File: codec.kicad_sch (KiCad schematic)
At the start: 27 parts, among them J10 FCR684204T, J11 DIN_DOUT_2TP, J13 AJ_TP5, J14 C_G0, J15 C_G7, J16 CRST, J17 C_CLKOUT, J5 RX0/RX1, U4 WM8805GEDS_V, Y2 12M

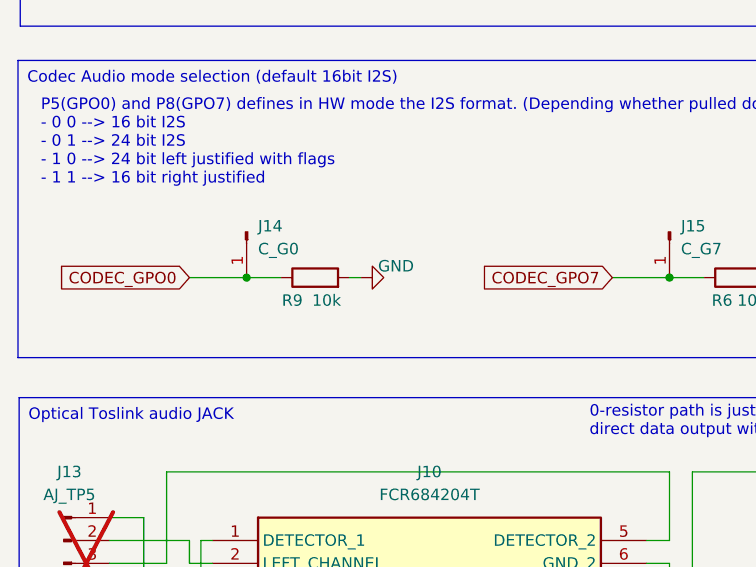
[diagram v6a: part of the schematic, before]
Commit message: component footprint updates
- 0402 caps and resistors to 0603
- reset pin-header to reset button

Signed-off-by: Mika Laitio <lamikr@gmail.com>
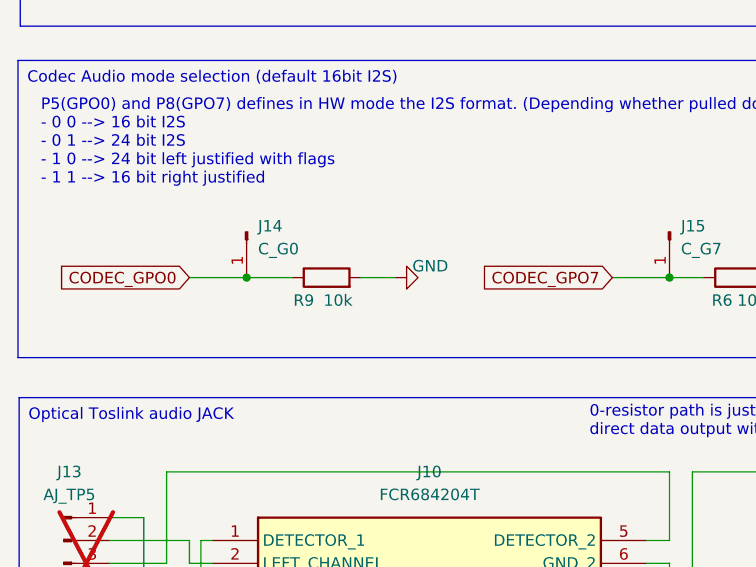
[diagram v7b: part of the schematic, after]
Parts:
- C17, C18, C19, C20, C21: footprint Capacitor_SMD:C_0402_1005Metric -> Capacitor_SMD:C_0603_1608Metric
- R6, R7, R8, R9: footprint Resistor_SMD:R_0402_1005Metric -> Resistor_SMD:R_0603_1608Metric
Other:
- moved on the sheet: R9
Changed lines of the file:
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@@
 	(wire
 		(pts
-			(xy 41.91 118.11) (xy 45.72 118.11)
+			(xy 41.91 118.11) (xy 46.99 118.11)
 		)
 		(stroke
@@
 	(wire
 		(pts
-			(xy 53.34 118.11) (xy 54.61 118.11)
+			(xy 54.61 118.11) (xy 58.42 118.11)
 		)
 		(stroke
@@
 			)
 		)
-		(property "Footprint" "Capacitor_SMD:C_0402_1005Metric"
+		(property "Footprint" "Capacitor_SMD:C_0603_1608Metric"
 			(at 64.4652 78.74 0)
 			(effects
@@
 			)
 		)
-		(property "Footprint" "Resistor_SMD:R_0402_1005Metric"
+		(property "Footprint" "Resistor_SMD:R_0603_1608Metric"
 			(at 58.42 57.658 90)
 			(effects
@@
 	(symbol
 		(lib_id "power:GND")
-		(at 54.61 118.11 90)
+		(at 58.42 118.11 90)
 		(unit 1)
 		(exclude_from_sim no)
@@
 		(dnp no)
 		(property "Reference" "#PWR029"
-			(at 60.96 118.11 0)
+			(at 64.77 118.11 0)
 			(effects
 				(font
@@
 		)
 		(property "Value" "GND"
-			(at 56.515 116.84 90)
+			(at 60.325 116.84 90)
 			(effects
 				(font
@@
 		)
 		(property "Footprint" ""
-			(at 54.61 118.11 0)
+			(at 58.42 118.11 0)
 			(effects
 				(font
@@
 		)
 		(property "Datasheet" ""
-			(at 54.61 118.11 0)
+			(at 58.42 118.11 0)
 			(effects
 				(font
@@
 		)
 		(property "Description" "Power symbol creates a global label with name \"GND\" , ground"
-			(at 54.61 118.11 0)
+			(at 58.42 118.11 0)
 			(effects
 				(font
@@
 			)
 		)
-		(property "Footprint" "Capacitor_SMD:C_0402_1005Metric"
+		(property "Footprint" "Capacitor_SMD:C_0603_1608Metric"
 			(at 256.54 137.4648 0)
 			(effects
@@
 			)
 		)
-		(property "Footprint" "Resistor_SMD:R_0402_1005Metric"
+		(property "Footprint" "Resistor_SMD:R_0603_1608Metric"
 			(at 181.61 117.348 90)
 			(effects
@@
 			)
 		)
-		(property "Footprint" "Capacitor_SMD:C_0402_1005Metric"
+		(property "Footprint" "Capacitor_SMD:C_0603_1608Metric"
 			(at 65.7352 33.02 0)
 			(effects
@@
 			)
 		)
-		(property "Footprint" "Capacitor_SMD:C_0402_1005Metric"
+		(property "Footprint" "Capacitor_SMD:C_0603_1608Metric"
 			(at 256.54 150.1648 0)
 			(effects
@@
 			)
 		)
-		(property "Footprint" "Resistor_SMD:R_0402_1005Metric"
+		(property "Footprint" "Resistor_SMD:R_0603_1608Metric"
 			(at 96.52 119.888 90)
 			(effects
@@
 			)
 		)
-		(property "Footprint" "Capacitor_SMD:C_0402_1005Metric"
+		(property "Footprint" "Capacitor_SMD:C_0603_1608Metric"
 			(at 92.4052 168.91 0)
 			(effects
@@
 	(symbol
 		(lib_id "Device:R")
-		(at 49.53 118.11 90)
+		(at 50.8 118.11 90)
 		(unit 1)
 		(exclude_from_sim no)
@@
 		(dnp no)
 		(property "Reference" "R9"
-			(at 46.99 120.65 90)
+			(at 48.26 120.65 90)
 			(effects
 				(font
@@
 		)
 		(property "Value" "10k"
-			(at 50.8 120.65 90)
+			(at 52.07 120.65 90)
 			(effects
 				(font
@@
 			)
 		)
-		(property "Footprint" "Resistor_SMD:R_0402_1005Metric"
-			(at 49.53 119.888 90)
+		(property "Footprint" "Resistor_SMD:R_0603_1608Metric"
+			(at 50.8 119.888 90)
 			(effects
 				(font
@@
 		)
 		(property "Datasheet" "~"
-			(at 49.53 118.11 0)
+			(at 50.8 118.11 0)
 			(effects
 				(font
@@
 		)
 		(property "Description" "Resistor"
-			(at 49.53 118.11 0)
+			(at 50.8 118.11 0)
 			(effects
 				(font
@@
 		)
 		(property "Notes" ""
-			(at 49.53 118.11 0)
+			(at 50.8 118.11 0)
 			(effects
 				(font
@@
 		)
 		(property "Price" "0.1"
-			(at 49.53 118.11 0)
+			(at 50.8 118.11 0)
 			(effects
 				(font
@@
 		)
 		(property "MFR" "Yageo"
-			(at 49.53 118.11 0)
+			(at 50.8 118.11 0)
 			(effects
 				(font
@@
 		)
 		(property "MPN" "RC0402FR-0710KL"
-			(at 49.53 118.11 0)
+			(at 50.8 118.11 0)
 			(effects
 				(font
@@
 		)
 		(property "SKU_DIGIKEY" "311-10.0KLRCT-ND"
-			(at 49.53 118.11 0)
+			(at 50.8 118.11 0)
 			(effects
 				(font
@@
 		)
 		(property "QtyOrdered" "100"
-			(at 49.53 118.11 0)
+			(at 50.8 118.11 0)
 			(effects
 				(font

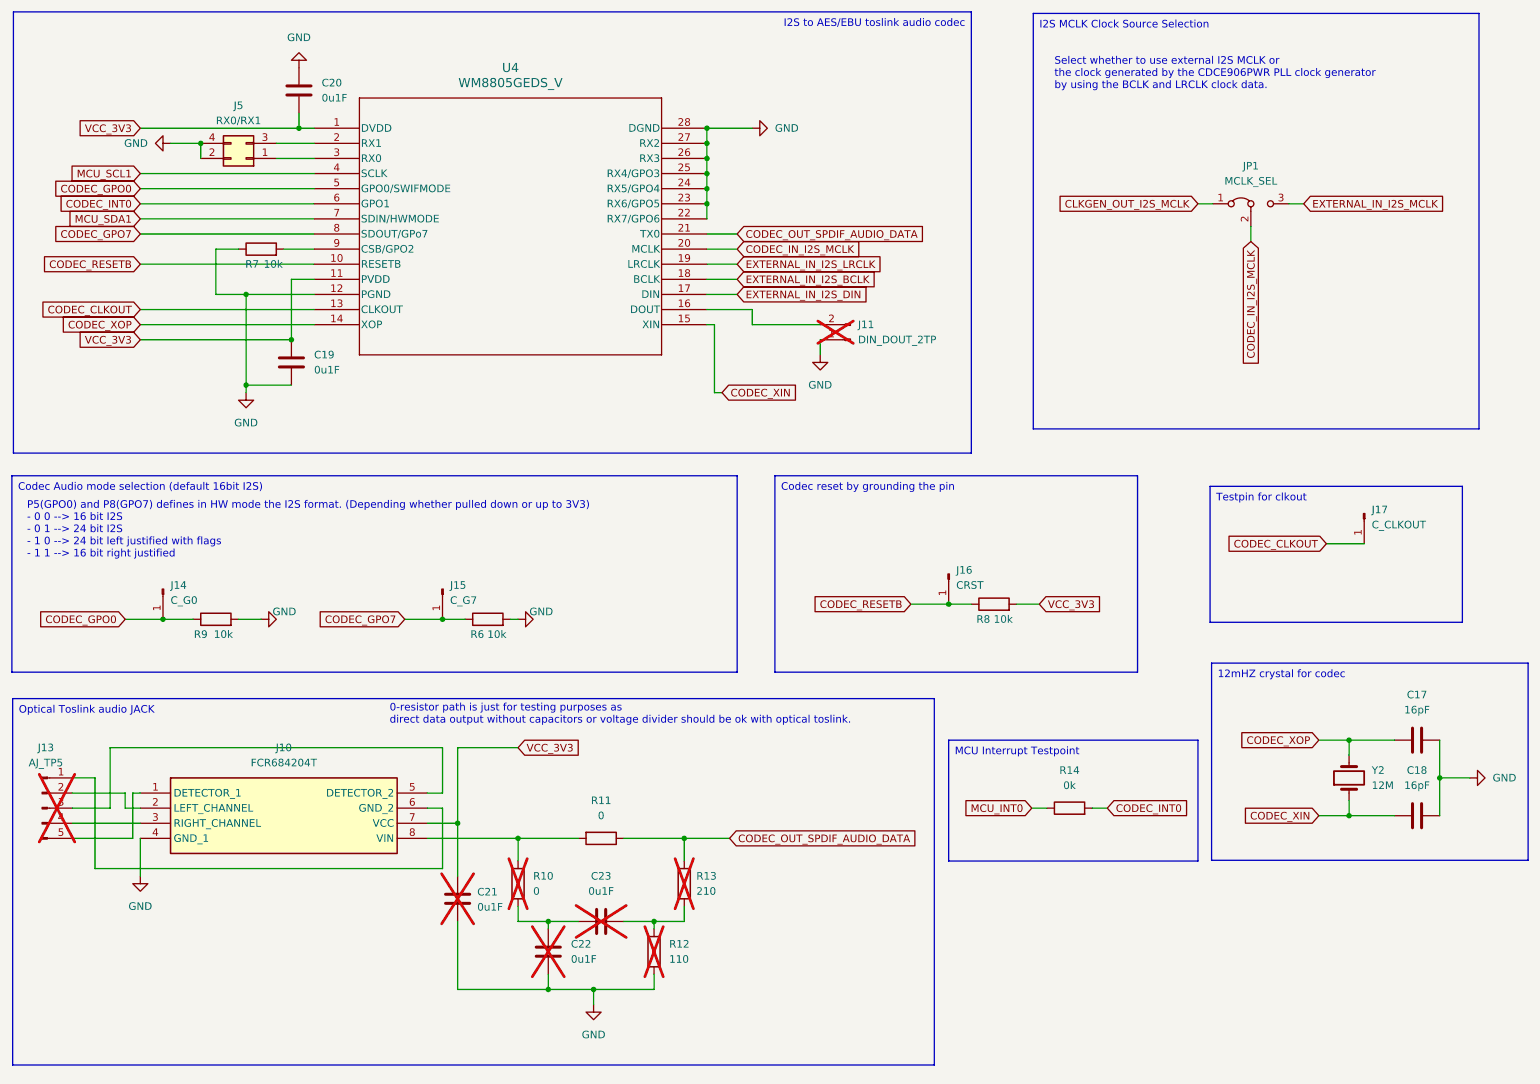
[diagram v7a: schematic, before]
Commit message: add pull-up resistors for codex rx-pins
- add connectors for rx0 and rx1 pins
- rest of the rx-pins not reserved for use
  and they will share a common pull-up.

Signed-off-by: Mika Laitio <lamikr@gmail.com>
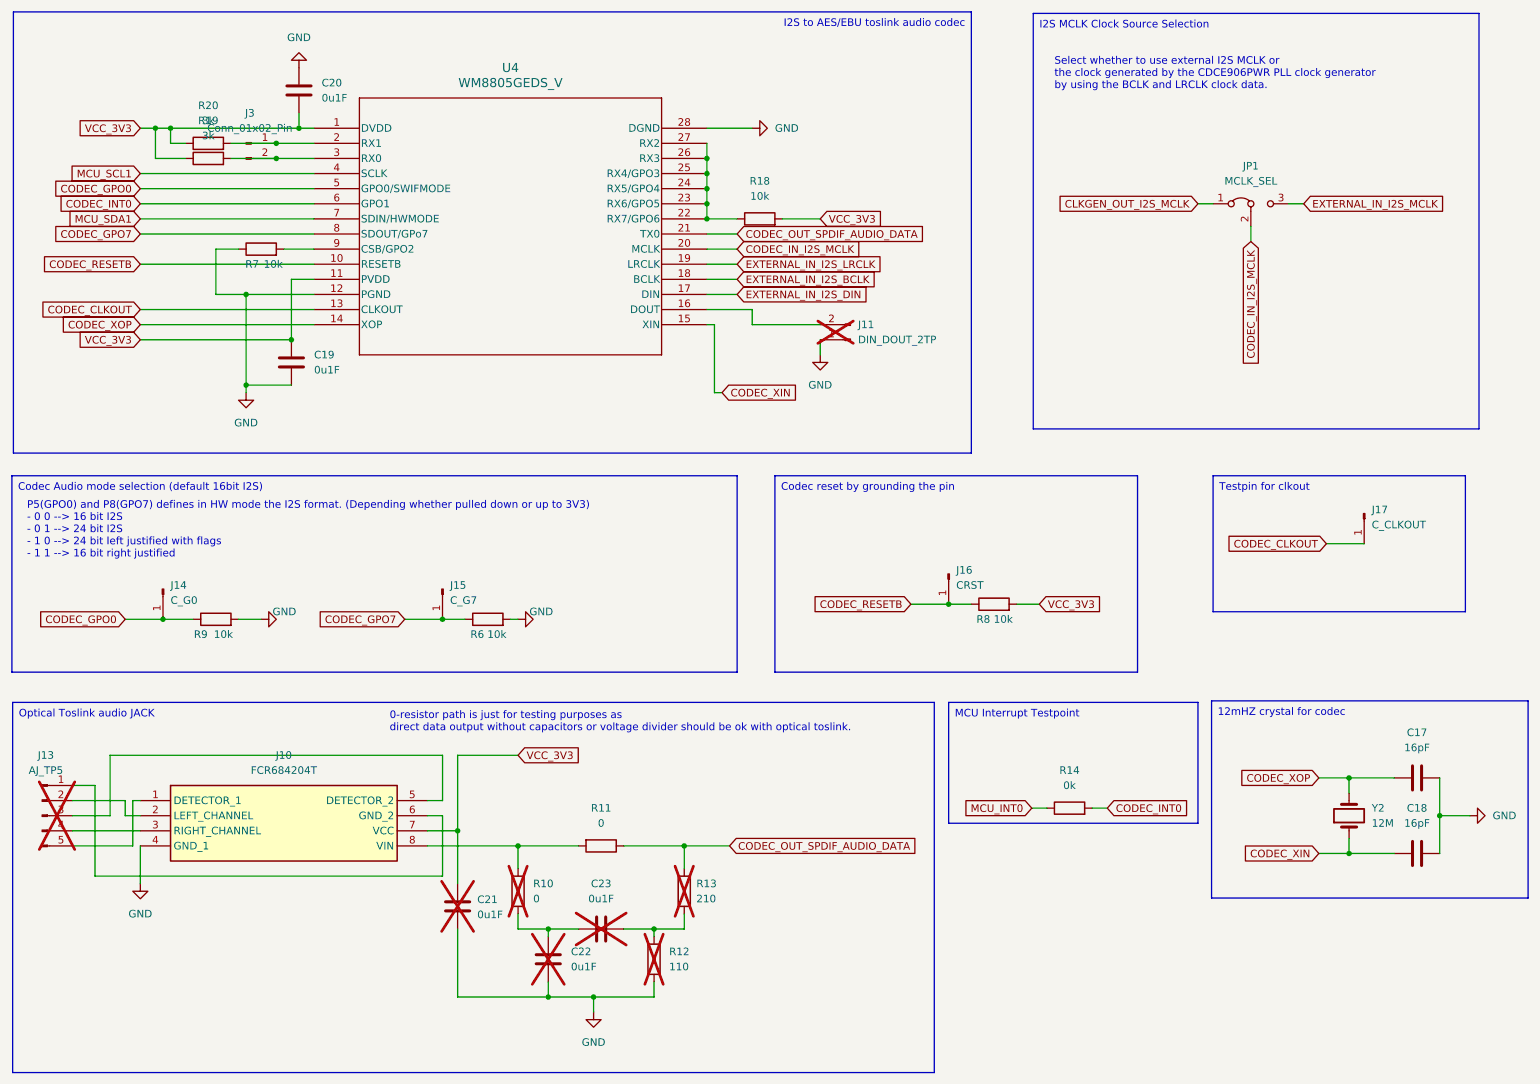
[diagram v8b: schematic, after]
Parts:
- removed J5: RX0/RX1, Connector_PinHeader_2.54mm:PinHeader_2x02_P2.54mm_Vertical, symbol Connector_Generic:Conn_02x02_Odd_Even
- added J3: Conn_01x02_Pin, Connector_PinHeader_2.54mm:PinHeader_1x02_P2.54mm_Vertical, symbol Connector:Conn_01x02_Pin
- added R18: 10k, Resistor_SMD:R_0603_1608Metric, symbol Device:R
- added R19, R20: 3k, Resistor_SMD:R_0603_1608Metric, symbol Device:R
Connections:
- net GND: no longer U4.22 (RX7/GPO6), U4.23 (RX6/GPO5), U4.24 (RX5/GPO4), U4.25 (RX4/GPO3), U4.26 (RX3), U4.27 (RX2)
- net VCC_3V3: now also R18.2, R19.1, R20.1
- net at U4.2 (RX1): now also J3.1 (Pin_1), R20.2
- net at U4.3 (RX0): now also J3.2 (Pin_2), R19.2
- new net: R18.1, U4.22 (RX7/GPO6), U4.23 (RX6/GPO5), U4.24 (RX5/GPO4), U4.25 (RX4/GPO3), U4.26 (RX3), U4.27 (RX2)
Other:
- moved on the sheet: C17, C18, C21, C22, C23, J10, J13, R10, R11, R12, R13, Y2
